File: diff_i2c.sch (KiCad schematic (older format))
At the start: 10 parts

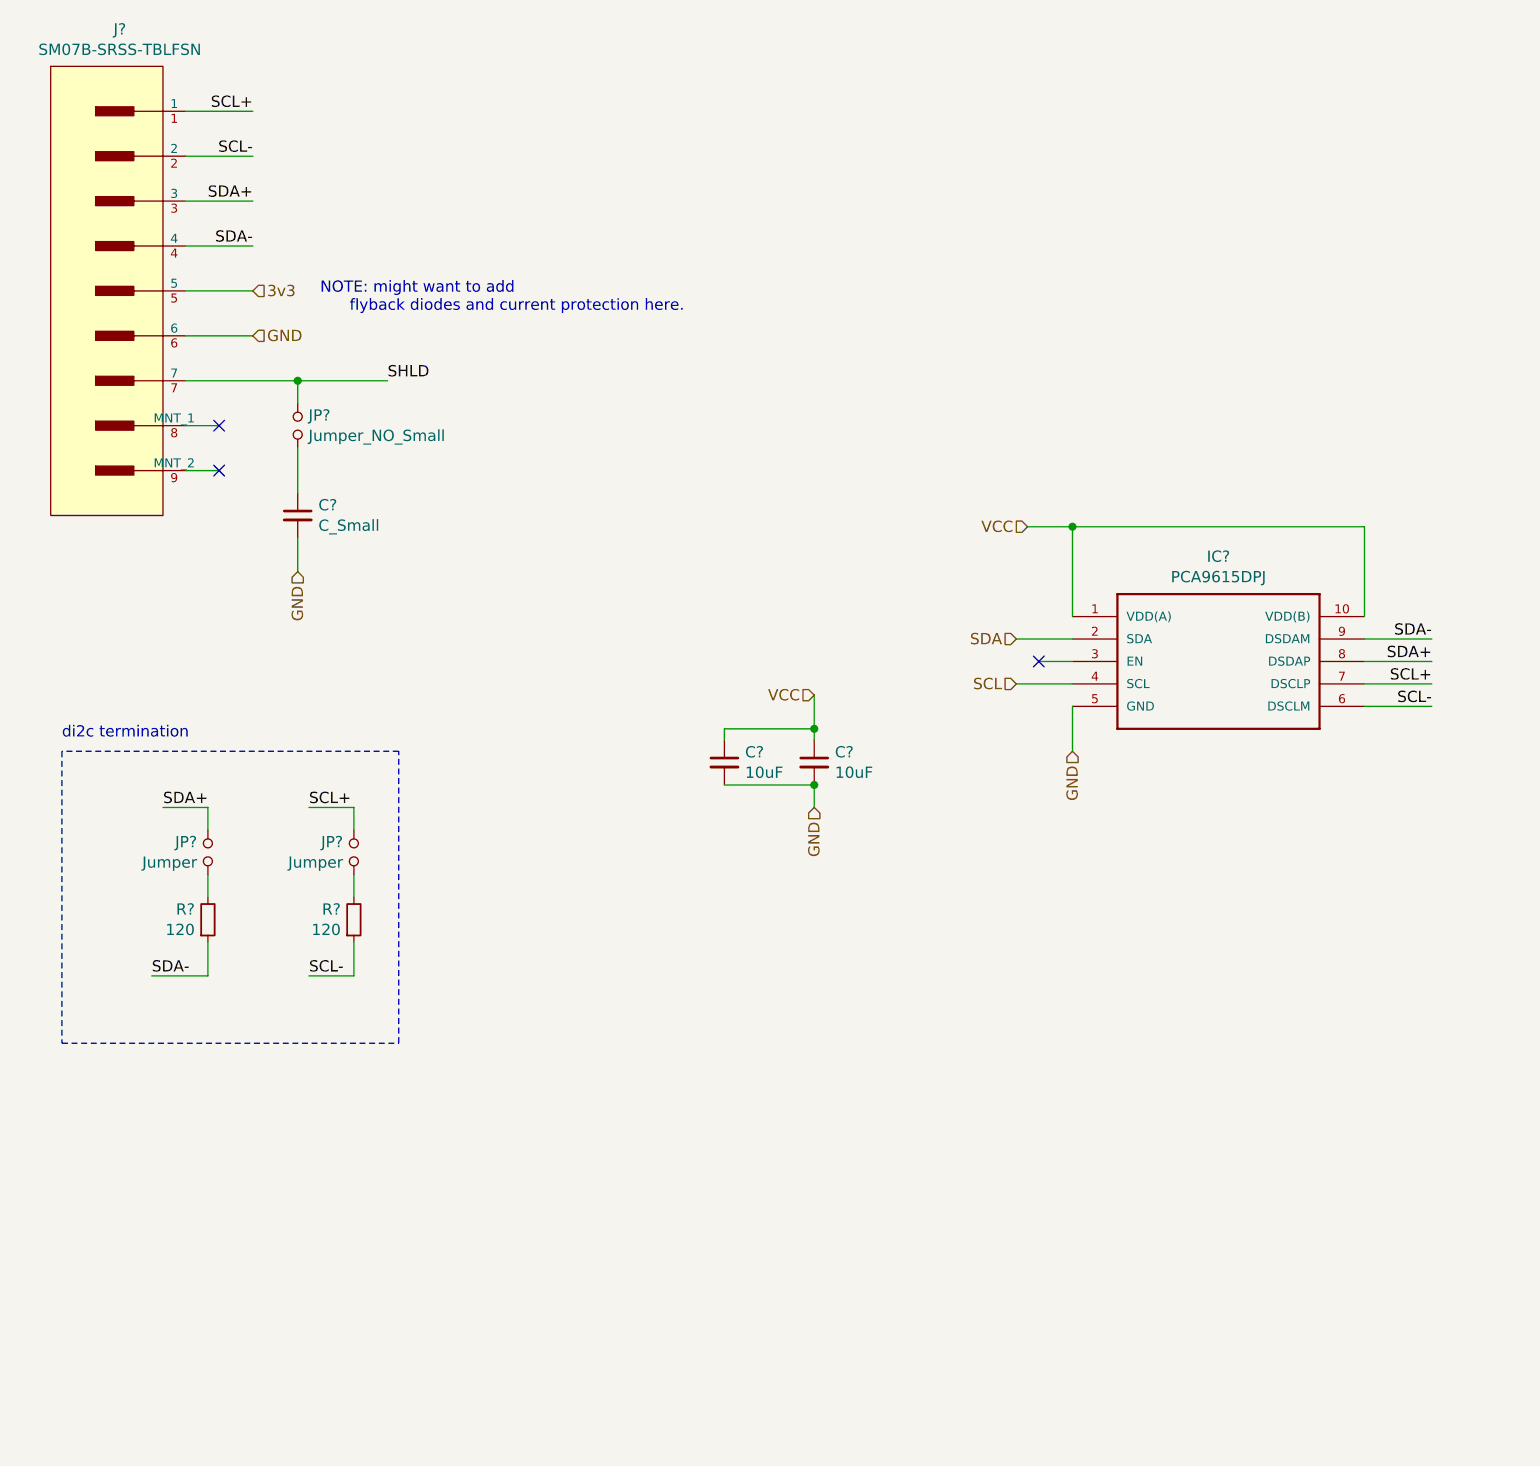
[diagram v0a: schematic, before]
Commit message: update reference ids, assign value to c8
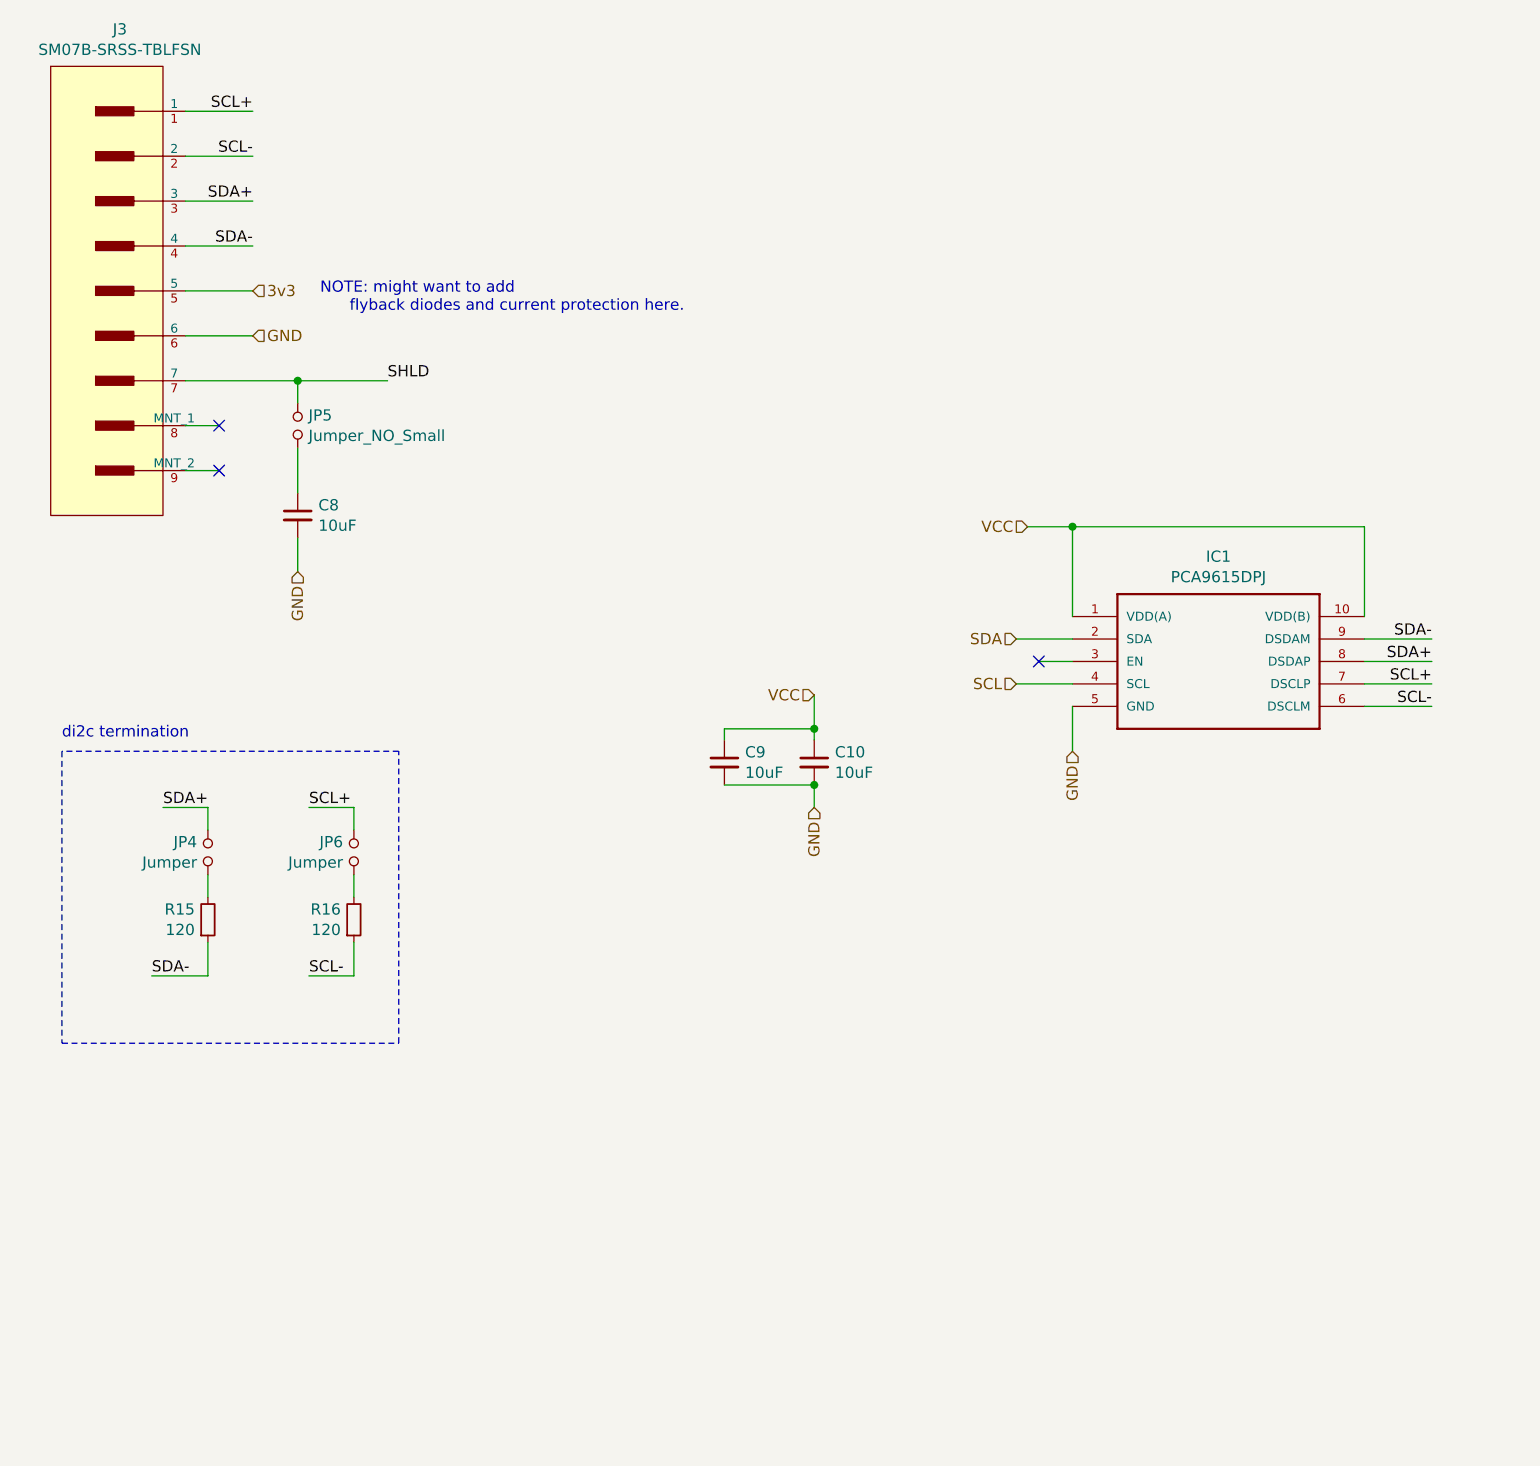
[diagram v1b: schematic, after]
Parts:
- C8: renamed from C?; value C_Small -> 10uF
- gave numbers to parts that had none: 9
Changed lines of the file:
@@
 $EndDescr
 $Comp
-L JST-SM07B-SRSS-TB:SM07B-SRSS-TBLFSN J?
+L JST-SM07B-SRSS-TB:SM07B-SRSS-TBLFSN J3
 U 1 1 61968298
 P 1600 1300
-F 0 "J?" H 1208 1665 50  0000 C CNN
+F 0 "J3" H 1208 1665 50  0000 C CNN
 F 1 "SM07B-SRSS-TBLFSN" H 1208 1574 50  0000 C CNN
 F 2 "JST-SM07B-SRSS-TBLFSN-*" H 1600 1800 50  0001 L CNN
@@
 	1500 2500 2000 2500
 $Comp
-L Device:Jumper_NO_Small JP?
+L Device:Jumper_NO_Small JP5
 U 1 1 6196BAC2
 P 2000 2700
-F 0 "JP?" V 2046 2652 50  0000 R CNN
+F 0 "JP5" V 2046 2652 50  0000 R CNN
 F 1 "Jumper_NO_Small" V 1955 2652 50  0000 R CNN
 F 2 "" H 2000 2700 50  0001 C CNN
@@
 	2000 2500 2400 2500
 $Comp
-L Device:C_Small C?
+L Device:C_Small C8
 U 1 1 6196BE9A
 P 2000 3100
-F 0 "C?" H 2092 3146 50  0000 L CNN
-F 1 "C_Small" H 2092 3055 50  0000 L CNN
+F 0 "C8" H 2092 3146 50  0000 L CNN
+F 1 "10uF" H 2092 3055 50  0000 L CNN
 F 2 "" H 2000 3100 50  0001 C CNN
 F 3 "~" H 2000 3100 50  0001 C CNN
@@
 NOTE: might want to add \n      flyback diodes and current protection here.
 $Comp
-L PCA9615:PCA9615DPJ IC?
+L PCA9615:PCA9615DPJ IC1
 U 1 1 61971D78
 P 5450 3550
-F 0 "IC?" H 6100 3817 50  0000 C CNN
+F 0 "IC1" H 6100 3817 50  0000 C CNN
 F 1 "PCA9615DPJ" H 6100 3726 50  0000 C CNN
 F 2 "SOP50P490X110-10N" H 5450 3550 50  0001 L BNN
@@
 	5450 3150 5450 3550
 $Comp
-L Device:C_Small C?
+L Device:C_Small C10
 U 1 1 6198DB03
 P 4300 4200
-F 0 "C?" H 4392 4246 50  0000 L CNN
+F 0 "C10" H 4392 4246 50  0000 L CNN
 F 1 "10uF" H 4392 4155 50  0000 L CNN
 F 2 "" H 4300 4200 50  0001 C CNN
@@
 	4300 4300 4300 4400
 $Comp
-L Device:C_Small C?
+L Device:C_Small C9
 U 1 1 61991791
 P 3900 4200
-F 0 "C?" H 3992 4246 50  0000 L CNN
+F 0 "C9" H 3992 4246 50  0000 L CNN
 F 1 "10uF" H 3992 4155 50  0000 L CNN
 F 2 "" H 3900 4200 50  0001 C CNN
@@
 P 1600 4600
 AR Path="/6187FA0A/61A12829" Ref="JP?"  Part="1"
-AR Path="/6195FE87/61A12829" Ref="JP?"  Part="1"
-F 0 "JP?" V 1554 4552 50  0000 R CNN
+AR Path="/6195FE87/61A12829" Ref="JP4"  Part="1"
+F 0 "JP4" V 1554 4552 50  0000 R CNN
 F 1 "Jumper" V 1645 4552 50  0000 R CNN
 F 2 "" H 1600 4600 50  0001 C CNN
@@
 P 1600 4900
 AR Path="/6187FA0A/61A1282F" Ref="R?"  Part="1"
-AR Path="/6195FE87/61A1282F" Ref="R?"  Part="1"
-F 0 "R?" H 1542 4854 50  0000 R CNN
+AR Path="/6195FE87/61A1282F" Ref="R15"  Part="1"
+F 0 "R15" H 1542 4854 50  0000 R CNN
 F 1 "120" H 1542 4945 50  0000 R CNN
 F 2 "" H 1600 4900 50  0001 C CNN
@@
 P 2250 4600
 AR Path="/6187FA0A/61A23D3B" Ref="JP?"  Part="1"
-AR Path="/6195FE87/61A23D3B" Ref="JP?"  Part="1"
-F 0 "JP?" V 2204 4552 50  0000 R CNN
+AR Path="/6195FE87/61A23D3B" Ref="JP6"  Part="1"
+F 0 "JP6" V 2204 4552 50  0000 R CNN
 F 1 "Jumper" V 2295 4552 50  0000 R CNN
 F 2 "" H 2250 4600 50  0001 C CNN
@@
 P 2250 4900
 AR Path="/6187FA0A/61A23D41" Ref="R?"  Part="1"
-AR Path="/6195FE87/61A23D41" Ref="R?"  Part="1"
-F 0 "R?" H 2192 4854 50  0000 R CNN
+AR Path="/6195FE87/61A23D41" Ref="R16"  Part="1"
+F 0 "R16" H 2192 4854 50  0000 R CNN
 F 1 "120" H 2192 4945 50  0000 R CNN
 F 2 "" H 2250 4900 50  0001 C CNN

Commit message: no longer a hat lol
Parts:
- added TP10, TP11, TP12, TP7, TP8, TP9: TestPoint, TestPoint:TestPoint_Pad_D2.5mm, symbol Connector:TestPoint
- C10, C8, C9: footprint (none) -> Capacitor_SMD:C_0805_2012Metric_Pad1.15x1.40mm_HandSolder
- IC1: footprint SOP50P490X110-10N -> PCA9615:PCA9615_SOP50P490
- J3: footprint JST-SM07B-SRSS-TBLFSN-* -> SM07B-SRSS-TB:JST-SM07B-SRSS-TBLFSN-0
- JP4, JP5, JP6: footprint (none) -> Connector_PinHeader_2.54mm:PinHeader_1x02_P2.54mm_Vertical
- R15, R16: footprint (none) -> Resistor_SMD:R_0805_2012Metric_Pad1.15x1.40mm_HandSolder
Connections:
- net 3v3 is gone; now on net VCC: J3.5
- net GND: now also TP8.1
- net SCL+: now also TP11.1
- net SCL-: now also TP12.1
- net SDA+: now also TP10.1
- net SDA-: now also TP9.1
- net VCC: now also TP7.1
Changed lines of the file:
@@
 F 0 "J3" H 1208 1665 50  0000 C CNN
 F 1 "SM07B-SRSS-TBLFSN" H 1208 1574 50  0000 C CNN
-F 2 "JST-SM07B-SRSS-TBLFSN-*" H 1600 1800 50  0001 L CNN
+F 2 "SM07B-SRSS-TB:JST-SM07B-SRSS-TBLFSN-0" H 1600 1800 50  0001 L CNN
 F 3 "https://upverter.com/datasheet/f612ce3c50b961849b9e0dc8dd6557d8d4d5c3c1.pdf" H 1600 1900 50  0001 L CNN
 F 4 "Tin" H 1600 2000 50  0001 L CNN "Contact Finish"
@@
 Wire Wire Line
 	1650 2700 1500 2700
-Text HLabel 1800 2100 2    50   Input ~ 0
-3v3
-Text HLabel 1800 2300 2    50   Input ~ 0
+Text HLabel 3250 2100 2    50   Input ~ 0
+VCC
+Text HLabel 3250 2300 2    50   Input ~ 0
 GND
 Wire Wire Line
@@
 F 0 "JP5" V 2046 2652 50  0000 R CNN
 F 1 "Jumper_NO_Small" V 1955 2652 50  0000 R CNN
-F 2 "" H 2000 2700 50  0001 C CNN
+F 2 "Connector_PinHeader_2.54mm:PinHeader_1x02_P2.54mm_Vertical" H 2000 2700 50  0001 C CNN
 F 3 "~" H 2000 2700 50  0001 C CNN
 	1    2000 2700
@@
 F 0 "C8" H 2092 3146 50  0000 L CNN
 F 1 "10uF" H 2092 3055 50  0000 L CNN
-F 2 "" H 2000 3100 50  0001 C CNN
+F 2 "Capacitor_SMD:C_0805_2012Metric_Pad1.15x1.40mm_HandSolder" H 2000 3100 50  0001 C CNN
 F 3 "~" H 2000 3100 50  0001 C CNN
 	1    2000 3100
@@
 Wire Wire Line
 	1500 1900 1800 1900
-Wire Wire Line
-	1500 2100 1800 2100
-Wire Wire Line
-	1500 2300 1800 2300
-Text Notes 2100 2200 0    50   ~ 0
+Text Notes 3550 2200 0    50   ~ 0
 NOTE: might want to add \n      flyback diodes and current protection here.
 $Comp
@@
 F 0 "IC1" H 6100 3817 50  0000 C CNN
 F 1 "PCA9615DPJ" H 6100 3726 50  0000 C CNN
-F 2 "SOP50P490X110-10N" H 5450 3550 50  0001 L BNN
+F 2 "PCA9615:PCA9615_SOP50P490" H 5450 3550 50  0001 L BNN
 F 3 "" H 5450 3550 50  0001 L BNN
 F 4 "NXP - PCA9615DPJ - BUFFER, DIFFERENTIAL I2C-BUS, TSSOP-10" H 5450 3550 50  0001 L BNN "Description"
@@
 F 0 "C10" H 4392 4246 50  0000 L CNN
 F 1 "10uF" H 4392 4155 50  0000 L CNN
-F 2 "" H 4300 4200 50  0001 C CNN
+F 2 "Capacitor_SMD:C_0805_2012Metric_Pad1.15x1.40mm_HandSolder" H 4300 4200 50  0001 C CNN
 F 3 "~" H 4300 4200 50  0001 C CNN
 	1    4300 4200
@@
 F 0 "C9" H 3992 4246 50  0000 L CNN
 F 1 "10uF" H 3992 4155 50  0000 L CNN
-F 2 "" H 3900 4200 50  0001 C CNN
+F 2 "Capacitor_SMD:C_0805_2012Metric_Pad1.15x1.40mm_HandSolder" H 3900 4200 50  0001 C CNN
 F 3 "~" H 3900 4200 50  0001 C CNN
 	1    3900 4200
@@
 Wire Wire Line
 	6750 3850 7050 3850
-Wire Wire Line
-	6750 3750 7050 3750
-Wire Wire Line
-	6750 3650 7050 3650
 Text Label 2400 2500 0    50   ~ 0
 SHLD
@@
 F 0 "JP4" V 1554 4552 50  0000 R CNN
 F 1 "Jumper" V 1645 4552 50  0000 R CNN
-F 2 "" H 1600 4600 50  0001 C CNN
+F 2 "Connector_PinHeader_2.54mm:PinHeader_1x02_P2.54mm_Vertical" H 1600 4600 50  0001 C CNN
 F 3 "~" H 1600 4600 50  0001 C CNN
 	1    1600 4600
@@
 F 0 "R15" H 1542 4854 50  0000 R CNN
 F 1 "120" H 1542 4945 50  0000 R CNN
-F 2 "" H 1600 4900 50  0001 C CNN
+F 2 "Resistor_SMD:R_0805_2012Metric_Pad1.15x1.40mm_HandSolder" H 1600 4900 50  0001 C CNN
 F 3 "~" H 1600 4900 50  0001 C CNN
 	1    1600 4900
@@
 F 0 "JP6" V 2204 4552 50  0000 R CNN
 F 1 "Jumper" V 2295 4552 50  0000 R CNN
-F 2 "" H 2250 4600 50  0001 C CNN
+F 2 "Connector_PinHeader_2.54mm:PinHeader_1x02_P2.54mm_Vertical" H 2250 4600 50  0001 C CNN
 F 3 "~" H 2250 4600 50  0001 C CNN
 	1    2250 4600
@@
 F 0 "R16" H 2192 4854 50  0000 R CNN
 F 1 "120" H 2192 4945 50  0000 R CNN
-F 2 "" H 2250 4900 50  0001 C CNN
+F 2 "Resistor_SMD:R_0805_2012Metric_Pad1.15x1.40mm_HandSolder" H 2250 4900 50  0001 C CNN
 F 3 "~" H 2250 4900 50  0001 C CNN
 	1    2250 4900
@@
 Text Label 1800 1900 2    50   ~ 0
 SDA-
+Wire Wire Line
+	6750 3750 7050 3750
+Wire Wire Line
+	6750 3650 7050 3650
+$Comp
+L Connector:TestPoint TP9
+U 1 1 61B8A771
+P 7050 3650
+F 0 "TP9" V 7050 3838 50  0000 L CNN
+F 1 "TestPoint" V 7095 3838 50  0001 L CNN
+F 2 "TestPoint:TestPoint_Pad_D2.5mm" H 7250 3650 50  0001 C CNN
+F 3 "~" H 7250 3650 50  0001 C CNN
+	1    7050 3650
+	0    1    1    0
+$EndComp
+$Comp
+L Connector:TestPoint TP10
+U 1 1 61B8ADC9
+P 7050 3750
+F 0 "TP10" V 7050 3938 50  0000 L CNN
+F 1 "TestPoint" V 7095 3938 50  0001 L CNN
+F 2 "TestPoint:TestPoint_Pad_D2.5mm" H 7250 3750 50  0001 C CNN
+F 3 "~" H 7250 3750 50  0001 C CNN
+	1    7050 3750
+	0    1    1    0
+$EndComp
+$Comp
+L Connector:TestPoint TP11
+U 1 1 61B8C5BF
+P 7050 3850
+F 0 "TP11" V 7050 4038 50  0000 L CNN
+F 1 "TestPoint" V 7095 4038 50  0001 L CNN
+F 2 "TestPoint:TestPoint_Pad_D2.5mm" H 7250 3850 50  0001 C CNN
+F 3 "~" H 7250 3850 50  0001 C CNN
+	1    7050 3850
+	0    1    1    0
+$EndComp
+$Comp
+L Connector:TestPoint TP12
+U 1 1 61B8C5C5
+P 7050 3950
+F 0 "TP12" V 7050 4138 50  0000 L CNN
+F 1 "TestPoint" V 7095 4138 50  0001 L CNN
+F 2 "TestPoint:TestPoint_Pad_D2.5mm" H 7250 3950 50  0001 C CNN
+F 3 "~" H 7250 3950 50  0001 C CNN
+	1    7050 3950
+	0    1    1    0
+$EndComp
+Wire Wire Line
+	1500 2100 3050 2100
+Wire Wire Line
+	1500 2300 3050 2300
+$Comp
+L Connector:TestPoint TP8
+U 1 1 61B915B9
+P 3050 2400
+F 0 "TP8" H 2992 2426 50  0000 R CNN
+F 1 "TestPoint" H 2992 2517 50  0000 R CNN
+F 2 "TestPoint:TestPoint_Pad_D2.5mm" H 3250 2400 50  0001 C CNN
+F 3 "~" H 3250 2400 50  0001 C CNN
+	1    3050 2400
+	-1   0    0    1
+$EndComp
+Wire Wire Line
+	3050 2400 3050 2300
+Connection ~ 3050 2300
+Wire Wire Line
+	3050 2300 3250 2300
+$Comp
+L Connector:TestPoint TP7
+U 1 1 61B932FB
+P 3050 2100
+F 0 "TP7" H 3108 2172 50  0000 L CNN
+F 1 "TestPoint" H 3108 2127 50  0001 L CNN
+F 2 "TestPoint:TestPoint_Pad_D2.5mm" H 3250 2100 50  0001 C CNN
+F 3 "~" H 3250 2100 50  0001 C CNN
+	1    3050 2100
+	1    0    0    -1
+$EndComp
+Connection ~ 3050 2100
+Wire Wire Line
+	3050 2100 3250 2100
 $EndSCHEMATC

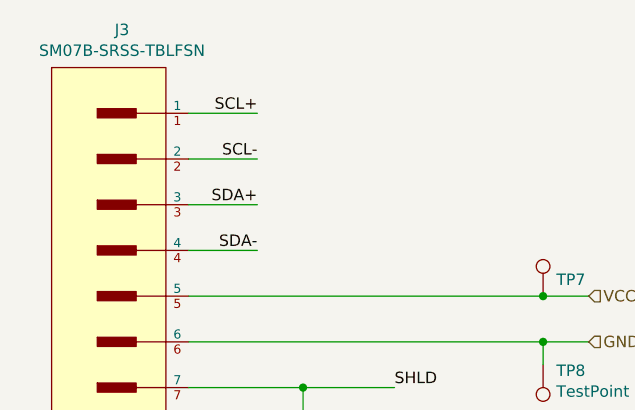
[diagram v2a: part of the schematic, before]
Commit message: [schematic] fix 3v3 symbol pin to use 3v3_pi instead of 5V_SRV
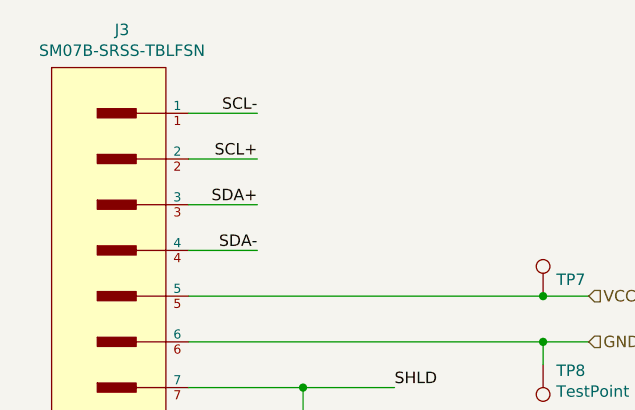
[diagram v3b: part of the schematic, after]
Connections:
- net SCL+: now also J3.2; no longer J3.1
- net SCL-: now also J3.1; no longer J3.2
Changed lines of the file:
@@
 SCL-
 Text Label 1800 1300 2    50   ~ 0
+SCL-
+Text Label 1800 1500 2    50   ~ 0
 SCL+
-Text Label 1800 1500 2    50   ~ 0
-SCL-
 Text Label 1800 1700 2    50   ~ 0
 SDA+
